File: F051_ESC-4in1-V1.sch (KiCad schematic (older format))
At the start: 20 parts, among them J1 Conn_01x02, J2 Conn_01x04, J3 Conn_01x04, J4 Conn_01x03, J5 Conn_01x04, J6 Conn_01x03, J7 Conn_01x03, J8 Conn_01x03

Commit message: Added the rest of the phases and their associated components
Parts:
- removed J2: Conn_01x04, Connector_JST:JST_SH_SM04B-SRSS-TB_1x04-1MP_P1.00mm_Horizontal, symbol Connector_Generic:Conn_01x04
- added C? (x18): 0.1uF, Capacitor_SMD:C_1206_3216Metric, symbol Device:C_Small
- added H? (x4): MountingHole_Pad, symbol Mechanical:MountingHole_Pad
- added J2: Conn_01x10, Connector_JST:JST_SHL_SM10B-SHLS-TF_1x10-1MP_P1.00mm_Horizontal, symbol Connector_Generic:Conn_01x10
- gave numbers to parts that had none: 6
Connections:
- net Curent Sense/CURR: now also J2.6 (Pin_6)
- net GND: now also C?.1, C?.1, C?.1, C?.1, C?.1, C?.1, C?.1, C?.1, C?.1, C?.1, C?.1, C?.1, C?.1, C?.1, C?.1, C?.1, C?.1, C?.1, H?.1, H?.1, H?.1, H?.1, J2.2 (Pin_2), J2.4 (Pin_4)
- net VCC_Shunt: now also C?.2, C?.2, C?.2, C?.2, C?.2, C?.2, C?.2, C?.2, C?.2, C?.2, C?.2, C?.2, C?.2, C?.2, C?.2, C?.2, C?.2, C?.2, J2.1 (Pin_1)
- new net +5V: J2.3 (Pin_3)
- new net PWM_1: J2.7 (Pin_7)
- new net PWM_2: J2.8 (Pin_8)
- new net PWM_3: J2.9 (Pin_9)
- new net PWM_4: J2.10 (Pin_10)
- no-connect marks 0 -> 1
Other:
- moved on the sheet: C16, C17, C18, C19, C20, C21, J1, J10, J11, J12, J13, J14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

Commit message: Added a test circuit to figure out best configuration
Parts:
- added J15: Conn_01x04, Connector_PinHeader_2.54mm:PinHeader_1x04_P2.54mm_Vertical, symbol Connector_Generic:Conn_01x04
- added J16: Conn_01x03, Connector_PinHeader_2.54mm:PinHeader_1x03_P2.54mm_Vertical, symbol Connector_Generic:Conn_01x03
- added J17: Conn_01x03, Connector_Wire:Conn_MotorPhase, symbol Connector_Generic:Conn_01x03
- H1, H2, H3, H4: renamed from H?; footprint (none) -> MountingHole:MountingHole_2.7mm_Pad
- gave numbers to parts that had none: 18
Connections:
- net +3V3: now also J15.1 (Pin_1)
- net GND: now also J15.2 (Pin_2)
- new net MCU Test/NRST: J16.1 (Pin_1)
- new net MCU Test/PhaseA: J17.3 (Pin_3)
- new net MCU Test/PhaseB: J17.2 (Pin_2)
- new net MCU Test/PhaseC: J17.1 (Pin_1)
- new net MCU Test/SWCLK: J15.3 (Pin_3)
- new net MCU Test/SWDIO: J15.4 (Pin_4)
- new net MCU Test/USART1_RX: J16.2 (Pin_2)
- new net MCU Test/USART1_TX: J16.3 (Pin_3)
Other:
- note added: "Motor Test"

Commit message: More design changes
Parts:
- removed J15: Conn_01x04, Connector_PinHeader_2.54mm:PinHeader_1x04_P2.54mm_Vertical, symbol Connector_Generic:Conn_01x04
- removed J16: Conn_01x03, Connector_PinHeader_2.54mm:PinHeader_1x03_P2.54mm_Vertical, symbol Connector_Generic:Conn_01x03
- removed J17: Conn_01x03, Connector_Wire:Conn_MotorPhase, symbol Connector_Generic:Conn_01x03
- J4: footprint Connector_Wire:Conn_MotorPhase -> Connector_PinHeader_2.54mm:PinHeader_1x03_P2.54mm_Vertical
- J6: footprint Connector_PinHeader_2.54mm:PinHeader_1x03_P2.54mm_Vertical -> Connector_Wire:Conn_MotorPhase
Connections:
- net MCU 1/NRST: now also J4.1 (Pin_1); no longer J6.1 (Pin_1)
- net MCU 1/PhaseA: now also J6.3 (Pin_3); no longer J4.3 (Pin_3)
- net MCU 1/PhaseB: now also J6.2 (Pin_2); no longer J4.2 (Pin_2)
- net MCU 1/PhaseC: now also J6.1 (Pin_1); no longer J4.1 (Pin_1)
- net MCU 1/USART1_RX: now also J4.2 (Pin_2); no longer J6.2 (Pin_2)
- net MCU 1/USART1_TX: now also J4.3 (Pin_3); no longer J6.3 (Pin_3)
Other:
- note removed: "Motor 4"
- note removed: "Motor Test"

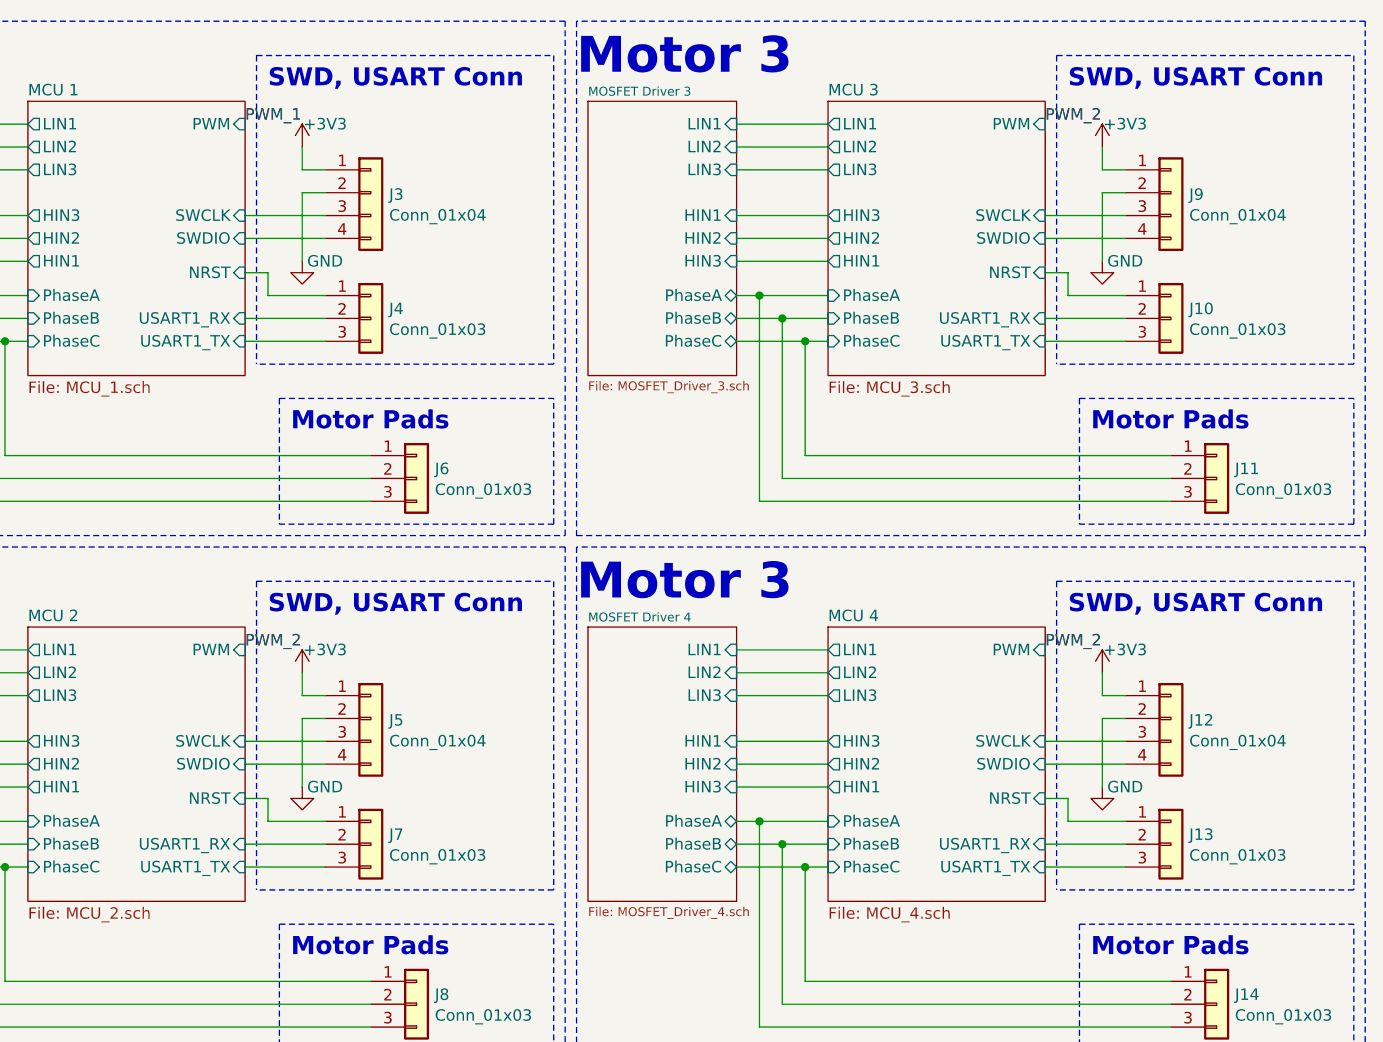
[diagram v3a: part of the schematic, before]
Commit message: Added pads for battery and debugging
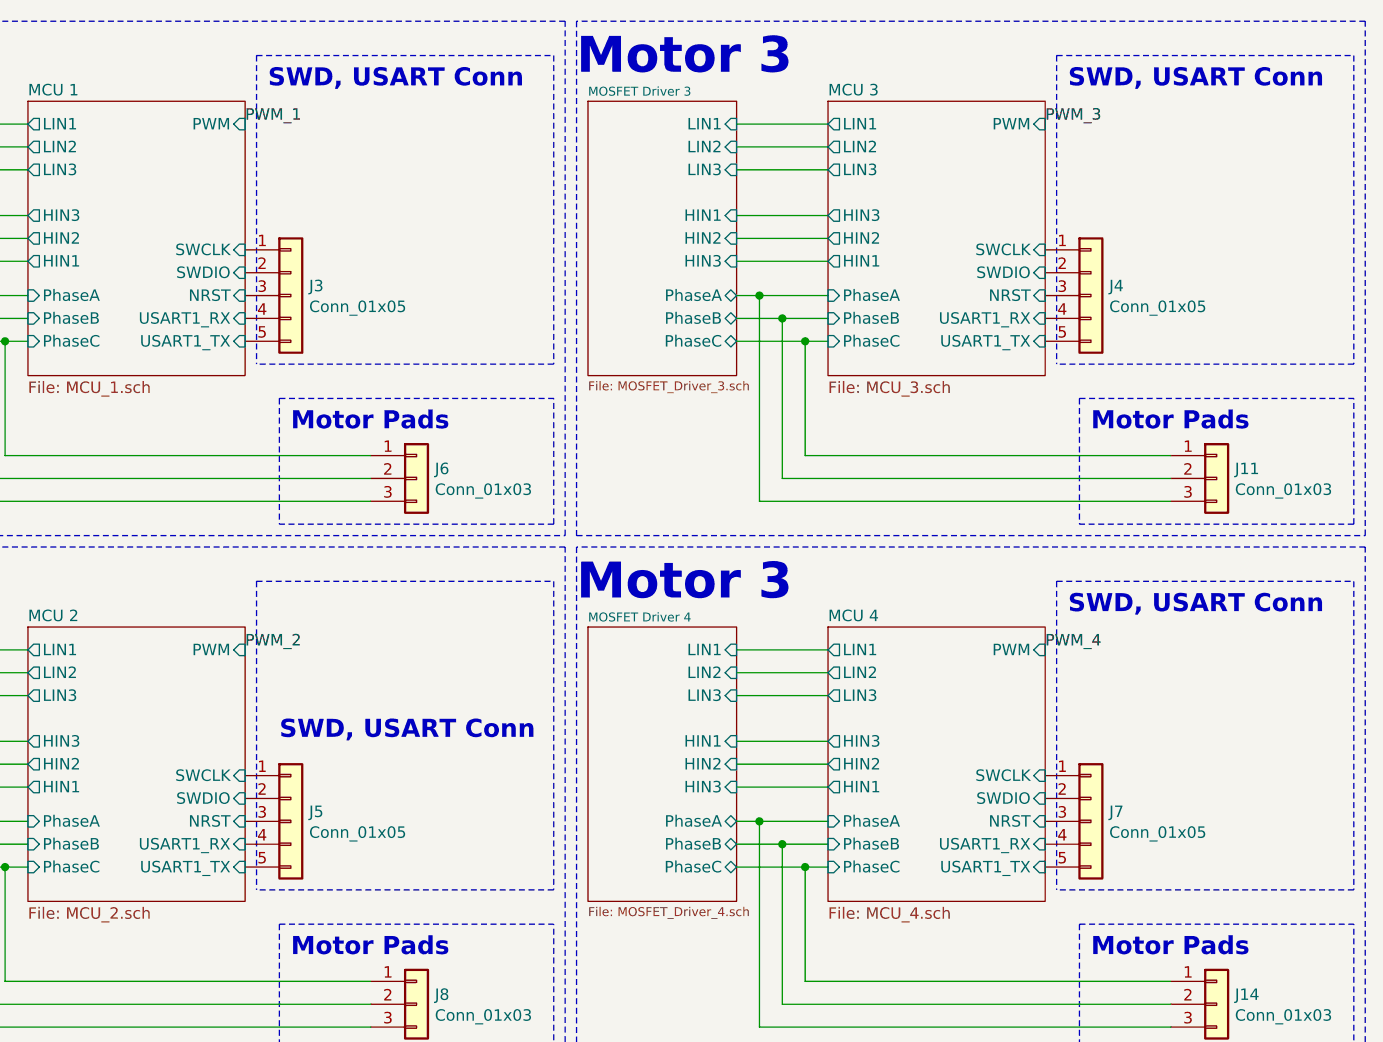
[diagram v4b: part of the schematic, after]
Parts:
- removed J10, J13, J4, J7: Conn_01x03, Connector_PinHeader_2.54mm:PinHeader_1x03_P2.54mm_Vertical, symbol Connector_Generic:Conn_01x03
- removed J12, J3, J5, J9: Conn_01x04, Connector_PinHeader_2.54mm:PinHeader_1x04_P2.54mm_Vertical, symbol Connector_Generic:Conn_01x04
- added J3, J4, J5, J7: Conn_01x05, Connector_Wire:Conn_Debug, symbol Connector_Generic:Conn_01x05
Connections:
- net MCU 1/NRST: now also J3.3 (Pin_3)
- net MCU 1/SWCLK: now also J3.1 (Pin_1)
- net MCU 1/SWDIO: now also J3.2 (Pin_2)
- net MCU 1/USART1_RX: now also J3.4 (Pin_4)
- net MCU 1/USART1_TX: now also J3.5 (Pin_5)
- net MCU 2/NRST: now also J5.3 (Pin_3)
- net MCU 2/SWCLK: now also J5.1 (Pin_1)
- net MCU 2/SWDIO: now also J5.2 (Pin_2)
- net MCU 2/USART1_RX: now also J5.4 (Pin_4)
- net MCU 2/USART1_TX: now also J5.5 (Pin_5)
- net MCU 3/NRST: now also J4.3 (Pin_3)
- net MCU 3/SWCLK: now also J4.1 (Pin_1)
- net MCU 3/SWDIO: now also J4.2 (Pin_2)
- net MCU 3/USART1_RX: now also J4.4 (Pin_4)
- net MCU 3/USART1_TX: now also J4.5 (Pin_5)
- net MCU 4/NRST: now also J7.3 (Pin_3)
- net MCU 4/SWCLK: now also J7.1 (Pin_1)
- net MCU 4/SWDIO: now also J7.2 (Pin_2)
- net MCU 4/USART1_RX: now also J7.4 (Pin_4)
- net MCU 4/USART1_TX: now also J7.5 (Pin_5)

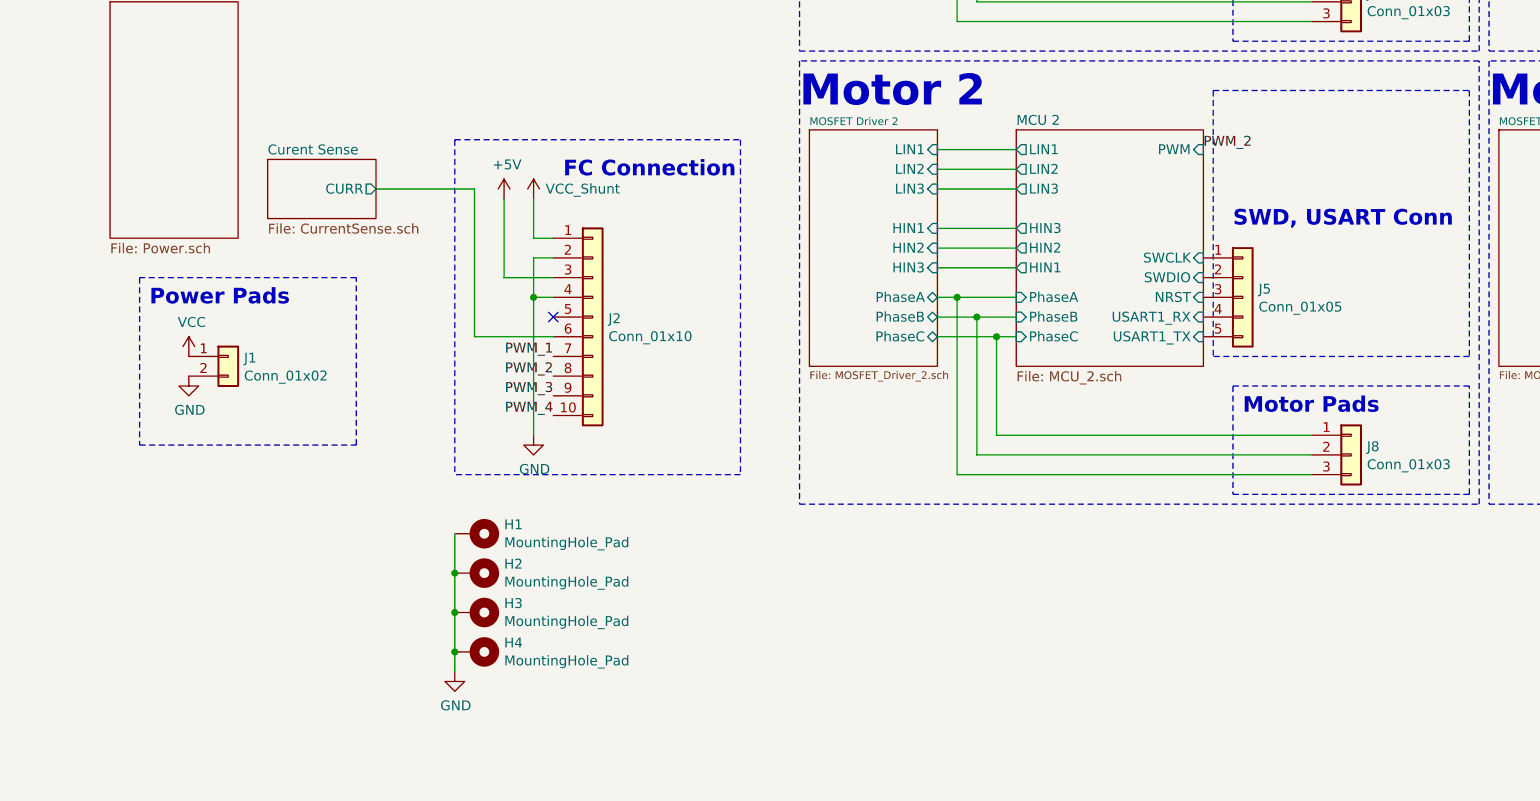
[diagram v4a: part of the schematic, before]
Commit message: Addition of 5V Regulator
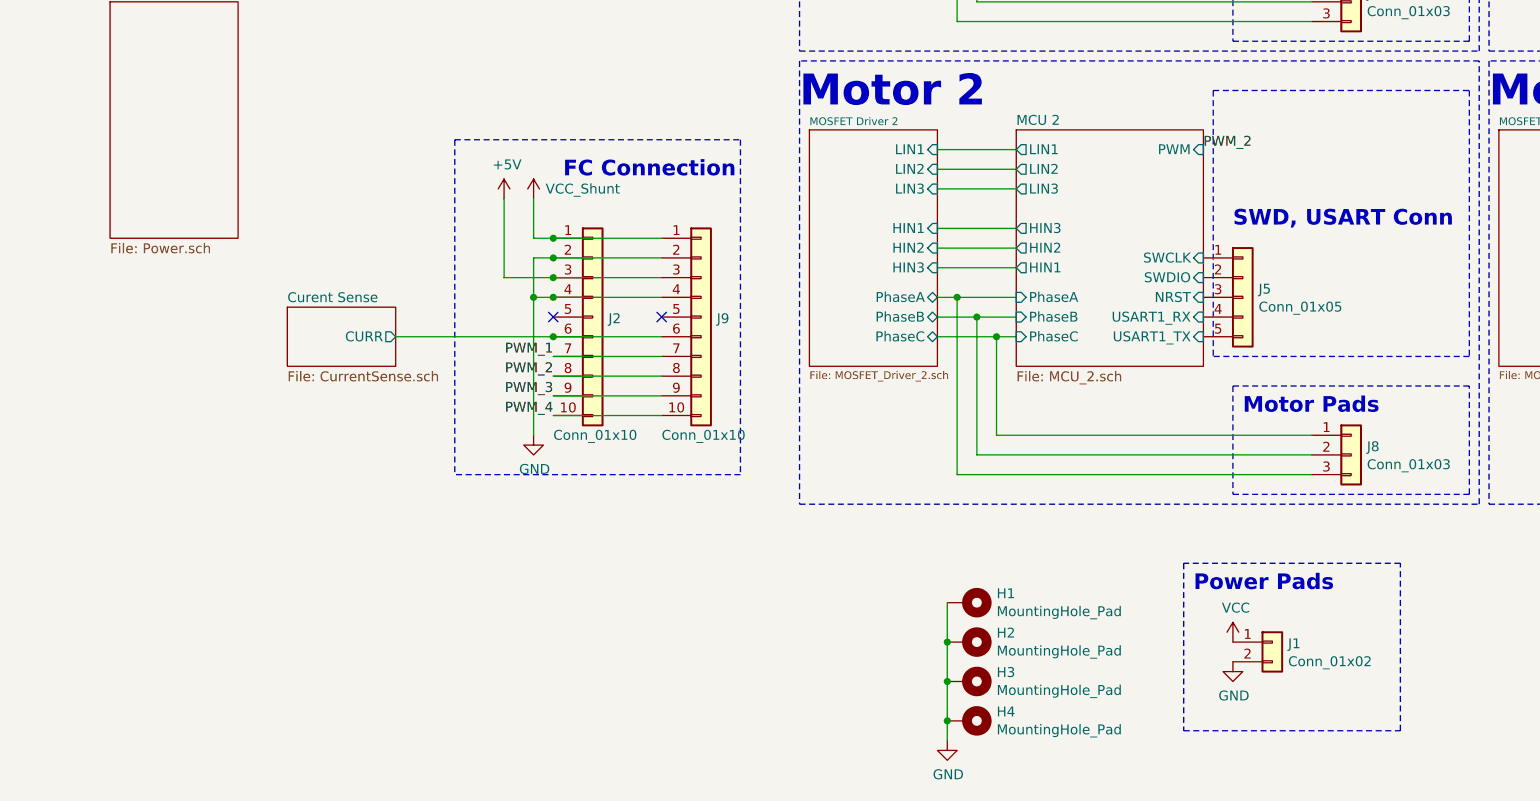
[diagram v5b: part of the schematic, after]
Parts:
- added J9: Conn_01x10, Connector_Wire:Conn_FC_Solder_10, symbol Connector_Generic:Conn_01x10
- H1, H2, H3, H4: footprint MountingHole:MountingHole_2.7mm_Pad -> MountingHole:MountingHole_4in1ESC
- J1: footprint Connector_Wire:Conn_PowerPad -> Connector_Wire:Conn_PowerPad_4in1
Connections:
- net +5V: now also J9.3 (Pin_3)
- net Curent Sense/CURR: now also J9.6 (Pin_6)
- net GND: now also J9.2 (Pin_2), J9.4 (Pin_4)
- net PWM_1: now also J9.7 (Pin_7)
- net PWM_2: now also J9.8 (Pin_8)
- net PWM_3: now also J9.9 (Pin_9)
- net PWM_4: now also J9.10 (Pin_10)
- net VCC_Shunt: now also J9.1 (Pin_1)
- no-connect marks 1 -> 2
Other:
- moved on the sheet: H1, H2, H3, H4, J1
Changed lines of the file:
@@
 L Connector_Generic:Conn_01x02 J1
 U 1 1 603AA048
-P 1300 4350
-F 0 "J1" H 1380 4342 50  0000 L CNN
-F 1 "Conn_01x02" H 1380 4251 50  0000 L CNN
-F 2 "Connector_Wire:Conn_PowerPad" H 1300 4350 50  0001 C CNN
-F 3 "~" H 1300 4350 50  0001 C CNN
-	1    1300 4350
+P 6600 5800
+F 0 "J1" H 6680 5792 50  0000 L CNN
+F 1 "Conn_01x02" H 6680 5701 50  0000 L CNN
+F 2 "Connector_Wire:Conn_PowerPad_4in1" H 6600 5800 50  0001 C CNN
+F 3 "~" H 6600 5800 50  0001 C CNN
+	1    6600 5800
 	1    0    0    -1
 $EndComp
@@
 L power:VCC #PWR0115
 U 1 1 603AAAE6
-P 1100 4350
-F 0 "#PWR0115" H 1100 4200 50  0001 C CNN
-F 1 "VCC" H 1115 4523 50  0000 C CNN
-F 2 "" H 1100 4350 50  0001 C CNN
-F 3 "" H 1100 4350 50  0001 C CNN
-	1    1100 4350
+P 6400 5800
+F 0 "#PWR0115" H 6400 5650 50  0001 C CNN
+F 1 "VCC" H 6415 5973 50  0000 C CNN
+F 2 "" H 6400 5800 50  0001 C CNN
+F 3 "" H 6400 5800 50  0001 C CNN
+	1    6400 5800
 	1    0    0    -1
 $EndComp
@@
 L power:GND #PWR0116
 U 1 1 603AAE97
-P 1100 4450
-F 0 "#PWR0116" H 1100 4200 50  0001 C CNN
-F 1 "GND" H 1105 4277 50  0000 C CNN
-F 2 "" H 1100 4450 50  0001 C CNN
-F 3 "" H 1100 4450 50  0001 C CNN
-	1    1100 4450
+P 6400 5900
+F 0 "#PWR0116" H 6400 5650 50  0001 C CNN
+F 1 "GND" H 6405 5727 50  0000 C CNN
+F 2 "" H 6400 5900 50  0001 C CNN
+F 3 "" H 6400 5900 50  0001 C CNN
+	1    6400 5900
 	1    0    0    -1
 $EndComp
@@
 Shunt Resistor and Input Filtering
 Wire Notes Line
-	850  4800 1950 4800
-Wire Notes Line
-	1950 4800 1950 3950
-Wire Notes Line
-	1950 3950 850  3950
-Wire Notes Line
-	850  3950 850  4800
-Text Notes 900  4100 0    79   ~ 16
+	6150 6250 7250 6250
+Wire Notes Line
+	7250 6250 7250 5400
+Wire Notes Line
+	7250 5400 6150 5400
+Wire Notes Line
+	6150 5400 6150 6250
+Text Notes 6200 5550 0    79   ~ 16
 Power Pads
 $Comp
@@
 Connection ~ 600  1450
 $Sheet
-S 1500 3350 550  300
+S 1600 4100 550  300
 U 60419849
 F0 "Curent Sense" 50
 F1 "CurrentSense.sch" 50
-F2 "CURR" O R 2050 3500 50
+F2 "CURR" O R 2150 4250 50
 $EndSheet
 $Comp
@@
 	1    0    0    -1
 $EndComp
-Wire Wire Line
-	2050 3500 2550 3500
 Wire Wire Line
 	4900 3300 5300 3300
@@
 P 3150 4150
 F 0 "J2" H 3230 4142 50  0000 L CNN
-F 1 "Conn_01x10" H 3230 4051 50  0000 L CNN
+F 1 "Conn_01x10" H 2950 3550 50  0000 L CNN
 F 2 "Connector_JST:JST_SHL_SM10B-SHLS-TF_1x10-1MP_P1.00mm_Horizontal" H 3150 4150 50  0001 C CNN
 F 3 "~" H 3150 4150 50  0001 C CNN
@@
 Wire Wire Line
 	2850 4050 2850 4750
-Wire Wire Line
-	2550 4250 2950 4250
-Wire Wire Line
-	2550 3500 2550 4250
 Text Label 2950 4350 2    50   ~ 0
 PWM_1
@@
 L Mechanical:MountingHole_Pad H1
 U 1 1 6052A9DD
-P 2550 5250
-F 0 "H1" V 2504 5400 50  0000 L CNN
-F 1 "MountingHole_Pad" V 2595 5400 50  0000 L CNN
-F 2 "MountingHole:MountingHole_2.7mm_Pad" H 2550 5250 50  0001 C CNN
-F 3 "~" H 2550 5250 50  0001 C CNN
-	1    2550 5250
+P 5050 5600
+F 0 "H1" V 5004 5750 50  0000 L CNN
+F 1 "MountingHole_Pad" V 5095 5750 50  0000 L CNN
+F 2 "MountingHole:MountingHole_4in1ESC" H 5050 5600 50  0001 C CNN
+F 3 "~" H 5050 5600 50  0001 C CNN
+	1    5050 5600
 	0    1    1    0
 $EndComp
@@
 L Mechanical:MountingHole_Pad H2
 U 1 1 6052B335
-P 2550 5450
-F 0 "H2" V 2504 5600 50  0000 L CNN
-F 1 "MountingHole_Pad" V 2595 5600 50  0000 L CNN
-F 2 "MountingHole:MountingHole_2.7mm_Pad" H 2550 5450 50  0001 C CNN
-F 3 "~" H 2550 5450 50  0001 C CNN
-	1    2550 5450
+P 5050 5800
+F 0 "H2" V 5004 5950 50  0000 L CNN
+F 1 "MountingHole_Pad" V 5095 5950 50  0000 L CNN
+F 2 "MountingHole:MountingHole_4in1ESC" H 5050 5800 50  0001 C CNN
+F 3 "~" H 5050 5800 50  0001 C CNN
+	1    5050 5800
 	0    1    1    0
 $EndComp
@@
 L Mechanical:MountingHole_Pad H3
 U 1 1 6052B821
-P 2550 5650
-F 0 "H3" V 2504 5800 50  0000 L CNN
-F 1 "MountingHole_Pad" V 2595 5800 50  0000 L CNN
-F 2 "MountingHole:MountingHole_2.7mm_Pad" H 2550 5650 50  0001 C CNN
-F 3 "~" H 2550 5650 50  0001 C CNN
-	1    2550 5650
+P 5050 6000
+F 0 "H3" V 5004 6150 50  0000 L CNN
+F 1 "MountingHole_Pad" V 5095 6150 50  0000 L CNN
+F 2 "MountingHole:MountingHole_4in1ESC" H 5050 6000 50  0001 C CNN
+F 3 "~" H 5050 6000 50  0001 C CNN
+	1    5050 6000
 	0    1    1    0
 $EndComp
@@
 L Mechanical:MountingHole_Pad H4
 U 1 1 6052BBCA
-P 2550 5850
-F 0 "H4" V 2504 6000 50  0000 L CNN
-F 1 "MountingHole_Pad" V 2595 6000 50  0000 L CNN
-F 2 "MountingHole:MountingHole_2.7mm_Pad" H 2550 5850 50  0001 C CNN
-F 3 "~" H 2550 5850 50  0001 C CNN
-	1    2550 5850
+P 5050 6200
+F 0 "H4" V 5004 6350 50  0000 L CNN
+F 1 "MountingHole_Pad" V 5095 6350 50  0000 L CNN
+F 2 "MountingHole:MountingHole_4in1ESC" H 5050 6200 50  0001 C CNN
+F 3 "~" H 5050 6200 50  0001 C CNN
+	1    5050 6200
 	0    1    1    0
 $EndComp
@@
 L power:GND #PWR0218
 U 1 1 6052C474
-P 2450 5950
-F 0 "#PWR0218" H 2450 5700 50  0001 C CNN
-F 1 "GND" H 2455 5777 50  0000 C CNN
-F 2 "" H 2450 5950 50  0001 C CNN
-F 3 "" H 2450 5950 50  0001 C CNN
-	1    2450 5950
-	1    0    0    -1
-$EndComp
-Wire Wire Line
-	2450 5950 2450 5850
-Connection ~ 2450 5450
-Wire Wire Line
-	2450 5450 2450 5250
-Connection ~ 2450 5650
-Wire Wire Line
-	2450 5650 2450 5450
-Connection ~ 2450 5850
-Wire Wire Line
-	2450 5850 2450 5650
+P 4950 6300
+F 0 "#PWR0218" H 4950 6050 50  0001 C CNN
+F 1 "GND" H 4955 6127 50  0000 C CNN
+F 2 "" H 4950 6300 50  0001 C CNN
+F 3 "" H 4950 6300 50  0001 C CNN
+	1    4950 6300
+	1    0    0    -1
+$EndComp
+Wire Wire Line
+	4950 6300 4950 6200
+Connection ~ 4950 5800
+Wire Wire Line
+	4950 5800 4950 5600
+Connection ~ 4950 6000
+Wire Wire Line
+	4950 6000 4950 5800
+Connection ~ 4950 6200
+Wire Wire Line
+	4950 6200 4950 6000
 Wire Wire Line
 	4900 1000 5300 1000
@@
 	1    0    0    -1
 $EndComp
+Wire Wire Line
+	2150 4250 2950 4250
+$Comp
+L Connector_Generic:Conn_01x10 J9
+U 1 1 6056FCA6
+P 3700 4150
+F 0 "J9" H 3780 4142 50  0000 L CNN
+F 1 "Conn_01x10" H 3500 3550 50  0000 L CNN
+F 2 "Connector_Wire:Conn_FC_Solder_10" H 3700 4150 50  0001 C CNN
+F 3 "~" H 3700 4150 50  0001 C CNN
+	1    3700 4150
+	1    0    0    -1
+$EndComp
+Wire Wire Line
+	2950 3750 3500 3750
+Connection ~ 2950 3750
+Wire Wire Line
+	3500 3850 2950 3850
+Connection ~ 2950 3850
+Wire Wire Line
+	2950 3950 3500 3950
+Connection ~ 2950 3950
+Wire Wire Line
+	2950 4050 3500 4050
+Connection ~ 2950 4050
+Wire Wire Line
+	2950 4250 3500 4250
+Connection ~ 2950 4250
+Wire Wire Line
+	3500 4350 2950 4350
+Wire Wire Line
+	2950 4450 3500 4450
+Wire Wire Line
+	2950 4550 3500 4550
+Wire Wire Line
+	3500 4650 2950 4650
+NoConn ~ 3500 4150
 $EndSCHEMATC
